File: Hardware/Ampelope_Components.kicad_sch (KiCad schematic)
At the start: 101 parts, among them J1 Conn_01x12_Male, J18 SWD_Header, J19 USB_B_Micro, J2 Conn_01x12_Male, J3 Conn_01x12_Male, J4 Conn_01x12_Male, J5 Eurorack_16_pin_power, Q1 MMBT3904, Q2 MMBT3904, Q3 MMBT3904, Q4 MMBT3904, Q5 MMBT3904, U1 STM32G431RB, U2 AS3364, U3 LM1117-3.3, U4 TL074, U5 TL074, U6 TL074, Y1 8MHz 20pF

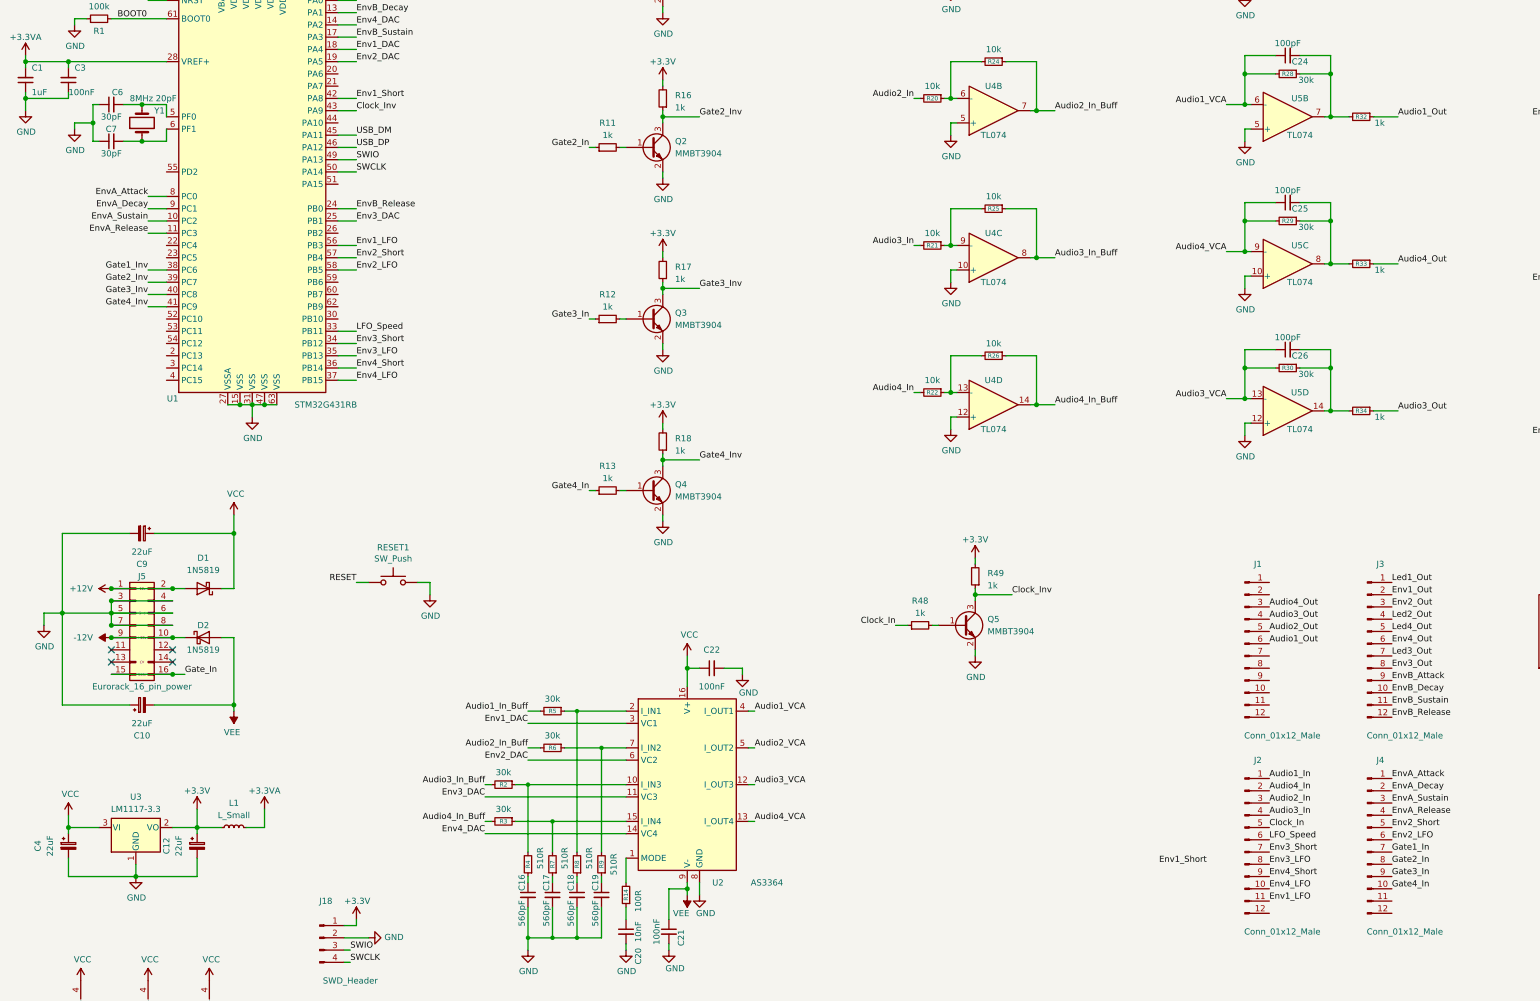
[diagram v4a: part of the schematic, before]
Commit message: Draft of panel layout
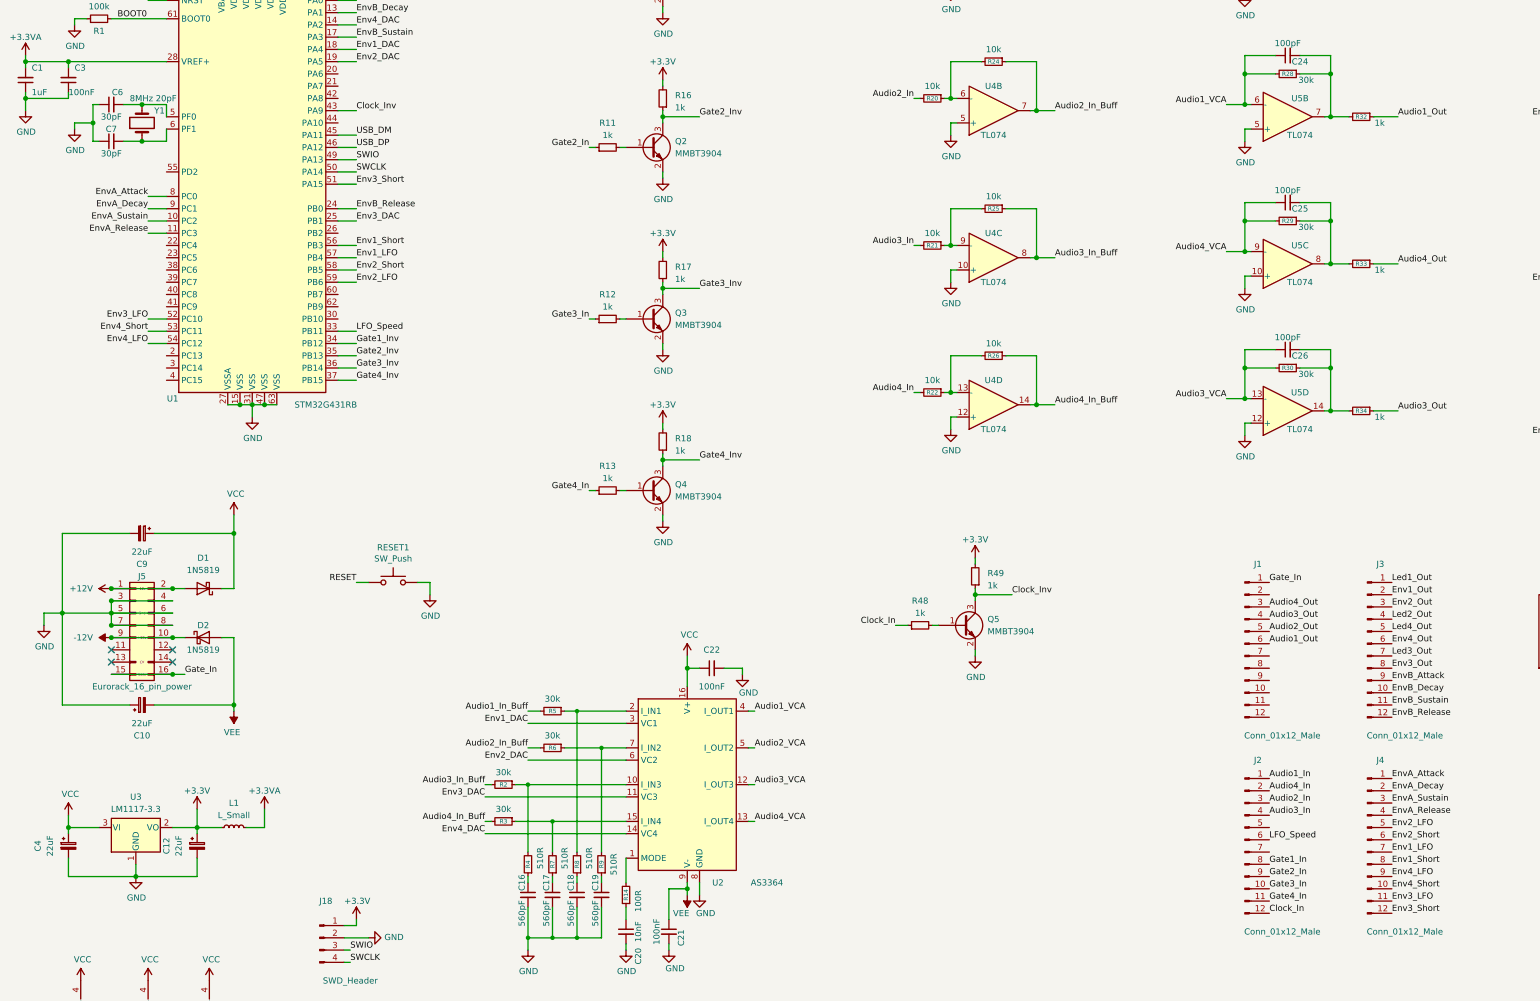
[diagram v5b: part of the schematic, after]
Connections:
- net Clock_In: now also J2.12 (Pin_12); no longer J2.5 (Pin_5)
- net Env1_LFO: now also J4.7 (Pin_7), U1.57 (PB4); no longer J2.11 (Pin_11), U1.56 (PB3)
- net Env1_Short: now also J4.8 (Pin_8), U1.56 (PB3); no longer U1.42 (PA8)
- net Env2_LFO: now also J4.5 (Pin_5), U1.59 (PB6); no longer J4.6 (Pin_6), U1.58 (PB5)
- net Env2_Short: now also J4.6 (Pin_6), U1.58 (PB5); no longer J4.5 (Pin_5), U1.57 (PB4)
- net Env3_LFO: now also J4.11 (Pin_11), U1.52 (PC10); no longer J2.8 (Pin_8), U1.35 (PB13)
- net Env3_Short: now also J4.12 (Pin_12), U1.51 (PA15); no longer J2.7 (Pin_7), U1.34 (PB12)
- net Env4_LFO: now also J4.9 (Pin_9), U1.54 (PC12); no longer J2.10 (Pin_10), U1.37 (PB15)
- net Env4_Short: now also J4.10 (Pin_10), U1.53 (PC11); no longer J2.9 (Pin_9), U1.36 (PB14)
- net Gate1_In: now also J2.8 (Pin_8); no longer J4.7 (Pin_7)
- net Gate1_Inv: now also U1.34 (PB12); no longer U1.38 (PC6)
- net Gate2_In: now also J2.9 (Pin_9); no longer J4.8 (Pin_8)
- net Gate2_Inv: now also U1.35 (PB13); no longer U1.39 (PC7)
- net Gate3_In: now also J2.10 (Pin_10); no longer J4.9 (Pin_9)
- net Gate3_Inv: now also U1.36 (PB14); no longer U1.40 (PC8)
- net Gate4_In: now also J2.11 (Pin_11); no longer J4.10 (Pin_10)
- net Gate4_Inv: now also U1.37 (PB15); no longer U1.41 (PC9)
- net Gate_In: now also J1.1 (Pin_1)
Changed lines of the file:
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@@
-(kicad_sch (version 20210621) (generator eeschema)
+(kicad_sch (version 20210615) (generator eeschema)
   (paper "A3")
   (junction (at 20.32 59.69) (diameter 1.016) (color 0 0 0 0))
@@
     (stroke (width 0) (type solid) (color 0 0 0 0))
   )
-  (wire (pts (xy 45.72 102.87) (xy 49.53 102.87))
-    (stroke (width 0) (type solid) (color 0 0 0 0))
-  )
-  (wire (pts (xy 45.72 105.41) (xy 49.53 105.41))
-    (stroke (width 0) (type solid) (color 0 0 0 0))
-  )
-  (wire (pts (xy 45.72 107.95) (xy 49.53 107.95))
-    (stroke (width 0) (type solid) (color 0 0 0 0))
-  )
-  (wire (pts (xy 45.72 110.49) (xy 49.53 110.49))
+  (wire (pts (xy 45.72 113.03) (xy 49.53 113.03))
+    (stroke (width 0) (type solid) (color 0 0 0 0))
+  )
+  (wire (pts (xy 45.72 115.57) (xy 49.53 115.57))
+    (stroke (width 0) (type solid) (color 0 0 0 0))
+  )
+  (wire (pts (xy 45.72 118.11) (xy 49.53 118.11))
     (stroke (width 0) (type solid) (color 0 0 0 0))
   )
@@
     (stroke (width 0) (type solid) (color 0 0 0 0))
   )
-  (wire (pts (xy 85.09 67.31) (xy 88.9 67.31))
-    (stroke (width 0) (type solid) (color 0 0 0 0))
-  )
   (wire (pts (xy 85.09 69.85) (xy 88.9 69.85))
     (stroke (width 0) (type solid) (color 0 0 0 0))
@@
     (stroke (width 0) (type solid) (color 0 0 0 0))
   )
+  (wire (pts (xy 85.09 105.41) (xy 88.9 105.41))
+    (stroke (width 0) (type solid) (color 0 0 0 0))
+  )
   (wire (pts (xy 85.09 115.57) (xy 88.9 115.57))
     (stroke (width 0) (type solid) (color 0 0 0 0))
@@
   )
   (wire (pts (xy 88.9 38.1) (xy 88.9 39.37))
+    (stroke (width 0) (type solid) (color 0 0 0 0))
+  )
+  (wire (pts (xy 88.9 85.09) (xy 85.09 85.09))
     (stroke (width 0) (type solid) (color 0 0 0 0))
   )
@@
     (effects (font (size 1.27 1.27)) (justify right bottom))
   )
-  (label "Gate1_Inv" (at 45.72 102.87 180)
-    (effects (font (size 1.27 1.27)) (justify right bottom))
-  )
-  (label "Gate2_Inv" (at 45.72 105.41 180)
-    (effects (font (size 1.27 1.27)) (justify right bottom))
-  )
-  (label "Gate3_Inv" (at 45.72 107.95 180)
-    (effects (font (size 1.27 1.27)) (justify right bottom))
-  )
-  (label "Gate4_Inv" (at 45.72 110.49 180)
+  (label "Env3_LFO" (at 45.72 113.03 180)
+    (effects (font (size 1.27 1.27)) (justify right bottom))
+  )
+  (label "Env4_Short" (at 45.72 115.57 180)
+    (effects (font (size 1.27 1.27)) (justify right bottom))
+  )
+  (label "Env4_LFO" (at 45.72 118.11 180)
     (effects (font (size 1.27 1.27)) (justify right bottom))
   )
@@
     (effects (font (size 1.27 1.27)) (justify left bottom))
   )
-  (label "Env1_Short" (at 88.9 67.31 0)
-    (effects (font (size 1.27 1.27)) (justify left bottom))
-  )
   (label "Clock_Inv" (at 88.9 69.85 0)
     (effects (font (size 1.27 1.27)) (justify left bottom))
@@
     (effects (font (size 1.27 1.27)) (justify left bottom))
   )
+  (label "Env3_Short" (at 88.9 85.09 0)
+    (effects (font (size 1.27 1.27)) (justify left bottom))
+  )
   (label "EnvB_Release" (at 88.9 90.17 0)
     (effects (font (size 1.27 1.27)) (justify left bottom))
@@
     (effects (font (size 1.27 1.27)) (justify left bottom))
   )
-  (label "Env1_LFO" (at 88.9 97.79 0)
-    (effects (font (size 1.27 1.27)) (justify left bottom))
-  )
-  (label "Env2_Short" (at 88.9 100.33 0)
-    (effects (font (size 1.27 1.27)) (justify left bottom))
-  )
-  (label "Env2_LFO" (at 88.9 102.87 0)
+  (label "Env1_Short" (at 88.9 97.79 0)
+    (effects (font (size 1.27 1.27)) (justify left bottom))
+  )
+  (label "Env1_LFO" (at 88.9 100.33 0)
+    (effects (font (size 1.27 1.27)) (justify left bottom))
+  )
+  (label "Env2_Short" (at 88.9 102.87 0)
+    (effects (font (size 1.27 1.27)) (justify left bottom))
+  )
+  (label "Env2_LFO" (at 88.9 105.41 0)
     (effects (font (size 1.27 1.27)) (justify left bottom))
   )
@@
     (effects (font (size 1.27 1.27)) (justify left bottom))
   )
-  (label "Env3_Short" (at 88.9 118.11 0)
-    (effects (font (size 1.27 1.27)) (justify left bottom))
-  )
-  (label "Env3_LFO" (at 88.9 120.65 0)
-    (effects (font (size 1.27 1.27)) (justify left bottom))
-  )
-  (label "Env4_Short" (at 88.9 123.19 0)
-    (effects (font (size 1.27 1.27)) (justify left bottom))
-  )
-  (label "Env4_LFO" (at 88.9 125.73 0)
+  (label "Gate1_Inv" (at 88.9 118.11 0)
+    (effects (font (size 1.27 1.27)) (justify left bottom))
+  )
+  (label "Gate2_Inv" (at 88.9 120.65 0)
+    (effects (font (size 1.27 1.27)) (justify left bottom))
+  )
+  (label "Gate3_Inv" (at 88.9 123.19 0)
+    (effects (font (size 1.27 1.27)) (justify left bottom))
+  )
+  (label "Gate4_Inv" (at 88.9 125.73 0)
     (effects (font (size 1.27 1.27)) (justify left bottom))
   )
@@
     (effects (font (size 1.27 1.27)) (justify left bottom))
   )
-  (label "Env1_Short" (at 255.27 226.06 0)
-    (effects (font (size 1.27 1.27)) (justify left bottom))
-  )
   (label "Audio2_VCA" (at 269.24 38.1 180)
     (effects (font (size 1.27 1.27)) (justify right bottom))
@@
     (effects (font (size 1.27 1.27)) (justify right bottom))
   )
+  (label "Gate_In" (at 278.13 167.64 0)
+    (effects (font (size 1.27 1.27)) (justify left bottom))
+  )
   (label "Audio4_Out" (at 278.13 172.72 0)
     (effects (font (size 1.27 1.27)) (justify left bottom))
@@
     (effects (font (size 1.27 1.27)) (justify left bottom))
   )
-  (label "Clock_In" (at 278.13 218.44 0)
-    (effects (font (size 1.27 1.27)) (justify left bottom))
-  )
   (label "LFO_Speed" (at 278.13 220.98 0)
     (effects (font (size 1.27 1.27)) (justify left bottom))
   )
-  (label "Env3_Short" (at 278.13 223.52 0)
-    (effects (font (size 1.27 1.27)) (justify left bottom))
-  )
-  (label "Env3_LFO" (at 278.13 226.06 0)
-    (effects (font (size 1.27 1.27)) (justify left bottom))
-  )
-  (label "Env4_Short" (at 278.13 228.6 0)
-    (effects (font (size 1.27 1.27)) (justify left bottom))
-  )
-  (label "Env4_LFO" (at 278.13 231.14 0)
-    (effects (font (size 1.27 1.27)) (justify left bottom))
-  )
-  (label "Env1_LFO" (at 278.13 233.68 0)
+  (label "Gate1_In" (at 278.13 226.06 0)
+    (effects (font (size 1.27 1.27)) (justify left bottom))
+  )
+  (label "Gate2_In" (at 278.13 228.6 0)
+    (effects (font (size 1.27 1.27)) (justify left bottom))
+  )
+  (label "Gate3_In" (at 278.13 231.14 0)
+    (effects (font (size 1.27 1.27)) (justify left bottom))
+  )
+  (label "Gate4_In" (at 278.13 233.68 0)
+    (effects (font (size 1.27 1.27)) (justify left bottom))
+  )
+  (label "Clock_In" (at 278.13 236.22 0)
     (effects (font (size 1.27 1.27)) (justify left bottom))
   )
@@
     (effects (font (size 1.27 1.27)) (justify left bottom))
   )
-  (label "Env2_Short" (at 303.53 218.44 0)
-    (effects (font (size 1.27 1.27)) (justify left bottom))
-  )
-  (label "Env2_LFO" (at 303.53 220.98 0)
-    (effects (font (size 1.27 1.27)) (justify left bottom))
-  )
-  (label "Gate1_In" (at 303.53 223.52 0)
-    (effects (font (size 1.27 1.27)) (justify left bottom))
-  )
-  (label "Gate2_In" (at 303.53 226.06 0)
-    (effects (font (size 1.27 1.27)) (justify left bottom))
-  )
-  (label "Gate3_In" (at 303.53 228.6 0)
-    (effects (font (size 1.27 1.27)) (justify left bottom))
-  )
-  (label "Gate4_In" (at 303.53 231.14 0)
-    (effects (font (size 1.27 1.27)) (justify left bottom))
-  )
+  (label "Env2_LFO" (at 303.53 218.44 0)
+    (effects (font (size 1.27 1.27)) (justify left bottom))
+  )
+  (label "Env2_Short" (at 303.53 220.98 0)
+    (effects (font (size 1.27 1.27)) (justify left bottom))
+  )
+  (label "Env1_LFO" (at 303.53 223.52 0)
+    (effects (font (size 1.27 1.27)) (justify left bottom))
+  )
+  (label "Env1_Short" (at 303.53 226.06 0)
+    (effects (font (size 1.27 1.27)) (justify left bottom))
+  )
+  (label "Env4_LFO" (at 303.53 228.6 0)
+    (effects (font (size 1.27 1.27)) (justify left bottom))
+  )
+  (label "Env4_Short" (at 303.53 231.14 0)
+    (effects (font (size 1.27 1.27)) (justify left bottom))
+  )
+  (label "Env3_LFO" (at 303.53 233.68 0)
+    (effects (font (size 1.27 1.27)) (justify left bottom))
+  )
+  (label "Env3_Short" (at 303.53 236.22 0)
+    (effects (font (size 1.27 1.27)) (justify left bottom))
+  )

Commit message: Layout on component board
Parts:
- RESET1: footprint Custom_Footprints:SW_PUSH_6mm_aligned -> Custom_Footprints:SW_SPST_EVQQ2
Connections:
- net Audio1_Out: now also J1.12 (Pin_12); no longer J1.6 (Pin_6)
- net Audio2_Out: now also J1.9 (Pin_9); no longer J1.5 (Pin_5)
- net Audio3_Out: now also J1.8 (Pin_8); no longer J1.4 (Pin_4)
- net Audio4_In: now also J2.6 (Pin_6); no longer J2.2 (Pin_2)
- net Audio4_Out: now also J1.7 (Pin_7); no longer J1.3 (Pin_3)
- net Env1_Out: now also J3.4 (Pin_4); no longer J3.2 (Pin_2)
- net Env2_Out: no longer J3.3 (Pin_3)
- net Env3_Out: now also J3.7 (Pin_7); no longer J3.8 (Pin_8)
- net Env4_Out: no longer J3.6 (Pin_6)
- net EnvB_Attack: now also J3.12 (Pin_12); no longer J3.9 (Pin_9)
- net EnvB_Decay: now also J3.11 (Pin_11); no longer J3.10 (Pin_10)
- net EnvB_Release: now also J3.9 (Pin_9); no longer J3.12 (Pin_12)
- net EnvB_Sustain: now also J3.10 (Pin_10); no longer J3.11 (Pin_11)
- net LFO_Speed: now also J2.7 (Pin_7); no longer J2.6 (Pin_6)
- net Led1_Out: now also J3.3 (Pin_3); no longer J3.1 (Pin_1)
- net Led2_Out: now also J3.5 (Pin_5); no longer J3.4 (Pin_4)
- net Led3_Out: now also J3.8 (Pin_8); no longer J3.7 (Pin_7)
- net Led4_Out: now also J3.6 (Pin_6); no longer J3.5 (Pin_5)
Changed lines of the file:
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@@
     (effects (font (size 1.27 1.27)) (justify left bottom))
   )
-  (label "Audio4_Out" (at 278.13 172.72 0)
+  (label "Audio4_Out" (at 278.13 182.88 0)
     (effects (font (size 1.27 1.27)) (justify left bottom))
   )
-  (label "Audio3_Out" (at 278.13 175.26 0)
+  (label "Audio3_Out" (at 278.13 185.42 0)
     (effects (font (size 1.27 1.27)) (justify left bottom))
   )
-  (label "Audio2_Out" (at 278.13 177.8 0)
+  (label "Audio2_Out" (at 278.13 187.96 0)
     (effects (font (size 1.27 1.27)) (justify left bottom))
   )
-  (label "Audio1_Out" (at 278.13 180.34 0)
+  (label "Audio1_Out" (at 278.13 195.58 0)
     (effects (font (size 1.27 1.27)) (justify left bottom))
   )
@@
     (effects (font (size 1.27 1.27)) (justify left bottom))
   )
-  (label "Audio4_In" (at 278.13 210.82 0)
-    (effects (font (size 1.27 1.27)) (justify left bottom))
-  )
   (label "Audio2_In" (at 278.13 213.36 0)
     (effects (font (size 1.27 1.27)) (justify left bottom))
@@
     (effects (font (size 1.27 1.27)) (justify left bottom))
   )
-  (label "LFO_Speed" (at 278.13 220.98 0)
+  (label "Audio4_In" (at 278.13 220.98 0)
+    (effects (font (size 1.27 1.27)) (justify left bottom))
+  )
+  (label "LFO_Speed" (at 278.13 223.52 0)
     (effects (font (size 1.27 1.27)) (justify left bottom))
   )
@@
     (effects (font (size 1.27 1.27)) (justify left bottom))
   )
-  (label "Led1_Out" (at 303.53 167.64 0)
-    (effects (font (size 1.27 1.27)) (justify left bottom))
-  )
-  (label "Env1_Out" (at 303.53 170.18 0)
-    (effects (font (size 1.27 1.27)) (justify left bottom))
-  )
-  (label "Env2_Out" (at 303.53 172.72 0)
+  (label "Led1_Out" (at 303.53 172.72 0)
     (effects (font (size 1.27 1.27)) (justify left bottom))
   )
-  (label "Led2_Out" (at 303.53 175.26 0)
+  (label "Env1_Out" (at 303.53 175.26 0)
     (effects (font (size 1.27 1.27)) (justify left bottom))
   )
-  (label "Led4_Out" (at 303.53 177.8 0)
+  (label "Led2_Out" (at 303.53 177.8 0)
     (effects (font (size 1.27 1.27)) (justify left bottom))
   )
-  (label "Env4_Out" (at 303.53 180.34 0)
+  (label "Led4_Out" (at 303.53 180.34 0)
     (effects (font (size 1.27 1.27)) (justify left bottom))
   )
-  (label "Led3_Out" (at 303.53 182.88 0)
+  (label "Env3_Out" (at 303.53 182.88 0)
     (effects (font (size 1.27 1.27)) (justify left bottom))
   )
-  (label "Env3_Out" (at 303.53 185.42 0)
+  (label "Led3_Out" (at 303.53 185.42 0)
     (effects (font (size 1.27 1.27)) (justify left bottom))
   )
-  (label "EnvB_Attack" (at 303.53 187.96 0)
+  (label "EnvB_Release" (at 303.53 187.96 0)
     (effects (font (size 1.27 1.27)) (justify left bottom))
   )
-  (label "EnvB_Decay" (at 303.53 190.5 0)
+  (label "EnvB_Sustain" (at 303.53 190.5 0)
     (effects (font (size 1.27 1.27)) (justify left bottom))
   )
-  (label "EnvB_Sustain" (at 303.53 193.04 0)
+  (label "EnvB_Decay" (at 303.53 193.04 0)
     (effects (font (size 1.27 1.27)) (justify left bottom))
   )
-  (label "EnvB_Release" (at 303.53 195.58 0)
+  (label "EnvB_Attack" (at 303.53 195.58 0)
     (effects (font (size 1.27 1.27)) (justify left bottom))
   )
@@
     (property "Reference" "RESET1" (id 0) (at 96.52 160.401 0))
     (property "Value" "SW_Push" (id 1) (at 96.52 162.7124 0))
-    (property "Footprint" "Custom_Footprints:SW_PUSH_6mm_aligned" (id 2) (at 96.52 162.56 0)
+    (property "Footprint" "Custom_Footprints:SW_SPST_EVQQ2" (id 2) (at 96.52 162.56 0)
       (effects (font (size 1.27 1.27)) hide)
     )
@@
     )
     (path "/7615093a-318c-4c05-a9b3-abeff2838590"
-      (reference "RESET1") (unit 1) (value "SW_Push") (footprint "Custom_Footprints:SW_PUSH_6mm_aligned")
+      (reference "RESET1") (unit 1) (value "SW_Push") (footprint "Custom_Footprints:SW_SPST_EVQQ2")
     )
     (path "/e59b611b-88be-4414-bef0-b655f1354de2"
